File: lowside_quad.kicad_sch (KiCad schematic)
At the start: 6 parts, among them U36 VNL5090, U37 VNL5090, U38 VNL5090, U39 VNL5090

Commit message: Published 1.5 gerbs, bom, cpl and pdf
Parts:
- renumbered RN9 to RN5, RN10 to RN6, U36 to U28, U37 to U29, U38 to U30, U39 to U31

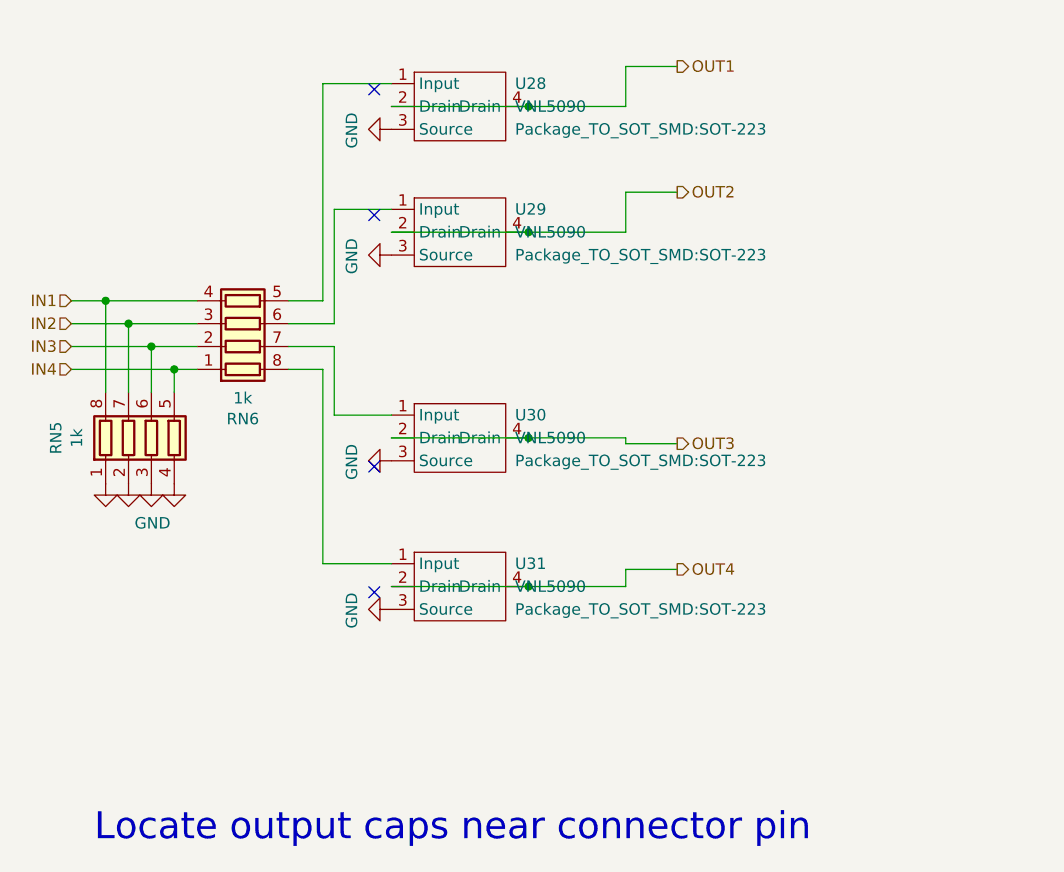
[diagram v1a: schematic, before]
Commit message: make hardware updates: - fix erc/drc errors - switch to VNLD5090 - switch to SOIC8 ignition drivers - BOM deduplication of similar parts
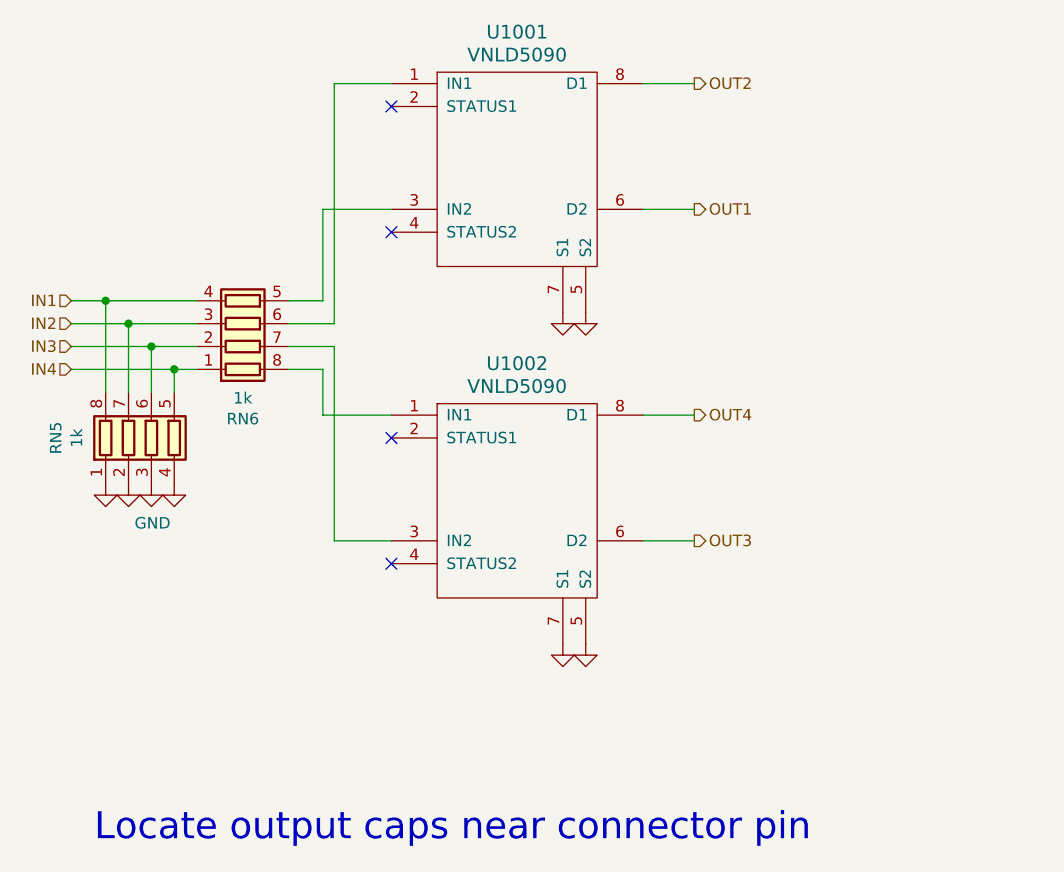
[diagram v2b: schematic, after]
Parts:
- removed U28, U29, U30, U31: VNL5090, Package_TO_SOT_SMD:SOT-223, symbol Simon:VNL5090
- added U1001, U1002: VNLD5090, Package_SO:SOIC-8_3.9x4.9mm_P1.27mm, symbol vnld5090:VNLD5090
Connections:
- net GND: now also U1001.5 (S2), U1001.7 (S1), U1002.5 (S2), U1002.7 (S1)
- net OUT1: now also U1001.6 (D2)
- net OUT2: now also U1001.8 (D1)
- net OUT3: now also U1002.6 (D2)
- net OUT4: now also U1002.8 (D1)
- net at RN6.5 (R4.2): now also U1001.3 (IN2)
- net at RN6.6 (R3.2): now also U1001.1 (IN1)
- net at RN6.7 (R2.2): now also U1002.3 (IN2)
- net at RN6.8 (R1.2): now also U1002.1 (IN1)
